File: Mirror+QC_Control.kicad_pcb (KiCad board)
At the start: 2 copper layers, 48.5 x 84 mm, 29 parts, among them J1 3220-10-0300-00, J2 Screw_Terminal_01x04, J3 Screw_Terminal_01x06, U1 LT1012, U10 LT1012, U11 LT1012, U2 LM4040DBZ-2.0, U3 LT1012, U4 LM4040DBZ-2.0, U5 LT1012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

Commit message: changes after DR1
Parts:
- added C10: 0.1muF, Capacitor_SMD:C_0805_2012Metric, F.Cu at (118.4, 38.3)
- added C11: 0.1muF, Capacitor_SMD:C_0805_2012Metric, F.Cu at (103.5, 88.4)
- added C12: 0.1muF, Capacitor_SMD:C_0805_2012Metric, F.Cu at (94.0, 100.5)
- added C13: 0.1muF, Capacitor_SMD:C_0805_2012Metric, F.Cu at (119.2, 98.4)
- added C14: 0.1muF, Capacitor_SMD:C_0805_2012Metric, F.Cu at (74.4, 113.8)
- added C15: 0.1muF, Capacitor_SMD:C_0805_2012Metric, F.Cu at (104.6, 115.5)
- added C16: C, Capacitor_SMD:C_0805_2012Metric, F.Cu at (115.4, 59.3)
- added C17: C, Capacitor_SMD:C_0805_2012Metric, F.Cu at (115.4, 91.4)
- added C18: C, Capacitor_SMD:C_0805_2012Metric, F.Cu at (117.3, 115.9)
- added C4: 0.1muF, Capacitor_SMD:C_0805_2012Metric, F.Cu at (93.1, 35.0)
- added C5: 0.1muF, Capacitor_SMD:C_0805_2012Metric, F.Cu at (74.2, 56.2)
- added C6: 0.1muF, Capacitor_SMD:C_0805_2012Metric, F.Cu at (105.5, 56.0)
- added C7: 0.1muF, Capacitor_SMD:C_0805_2012Metric, F.Cu at (96.5, 72.5)
- added C8: 0.1muF, Capacitor_SMD:C_0805_2012Metric, F.Cu at (119.5, 69.9)
- added C9: 0.1muF, Capacitor_SMD:C_0805_2012Metric, F.Cu at (76.5, 88.9)
- added D1: 5962-XL-2012UGCTR-ND, LED_SMD:LED_0805_2012Metric, F.Cu at (38.0, 117.0)
- added D2: 5962-XL-2012UGCTR-ND, LED_SMD:LED_0805_2012Metric, F.Cu at (38.0, 112.5)
- added D3: 5962-XL-2012UGCTR-ND, LED_SMD:LED_0805_2012Metric, F.Cu at (37.9, 107.5)
- added GND: TestPoint, TestPoint:TestPoint_Pad_2.0x2.0mm, F.Cu at (111.0, 117.0)
- added GND: TestPoint, TestPoint:TestPoint_Pad_2.0x2.0mm, F.Cu at (107.5, 62.5)
- added GND: TestPoint, TestPoint:TestPoint_Pad_2.0x2.0mm, F.Cu at (110.5, 91.5)
- added H1: MountingHole_Pad_MP, MountingHole:MountingHole_3.2mm_M3_DIN965_Pad_TopBottom, F.Cu at (26.0, 33.0)
- added H2: MountingHole_Pad_MP, MountingHole:MountingHole_3.2mm_M3_DIN965_Pad_TopBottom, F.Cu at (25.5, 114.0)
- added H3: MountingHole_Pad_MP, MountingHole:MountingHole_3.2mm_M3_DIN965_Pad_TopBottom, F.Cu at (167.5, 30.5)
- added H4: MountingHole_Pad_MP, MountingHole:MountingHole_3.2mm_M3_DIN965_Pad_TopBottom, F.Cu at (166.0, 113.5)
- added R13: 1300, Resistor_SMD:R_0805_2012Metric, F.Cu at (43.2, 117.0)
- added R14: 1300, Resistor_SMD:R_0805_2012Metric, F.Cu at (43.0, 112.5)
- added R17: 300, Resistor_SMD:R_0805_2012Metric, F.Cu at (43.0, 107.5)
- added SUM: 0-(-3.3V): TestPoint, TestPoint:TestPoint_Pad_2.0x2.0mm, F.Cu at (95.0, 112.0)
- added SUM: 0-3.3V: TestPoint, TestPoint:TestPoint_Pad_2.0x2.0mm, F.Cu at (126.7, 116.4)
- added X: 0-(-3.3V): TestPoint, TestPoint:TestPoint_Pad_2.0x2.0mm, F.Cu at (95.5, 56.5)
- added X: 0-3.3V: TestPoint, TestPoint:TestPoint_Pad_2.0x2.0mm, F.Cu at (127.1, 56.5)
- added Y: 0-(-3.3V): TestPoint, TestPoint:TestPoint_Pad_2.0x2.0mm, F.Cu at (96.5, 82.5)
- added Y: 0-3.3V: TestPoint, TestPoint:TestPoint_Pad_2.0x2.0mm, F.Cu at (127.5, 87.4)
- J1: value 3220-10-0300-00 -> FSM
- moved U11 119.2 mm to (115.5, 44.4), turned to 0 degrees
- moved U2 115.5 mm to (62.1, 44.6)
- moved R3 112.8 mm to (71.2, 43.6), turned to 0 degrees
- moved R5 103.9 mm to (105.1, 43.5), turned to 0 degrees
- moved R6 103.2 mm to (115.5, 55.5), turned to 0 degrees
- moved U10 102.3 mm to (88.2, 44.1), turned to 0 degrees
- moved J1 101.3 mm to (156.5, 85.0), turned to -90 degrees
- moved U7 98.7 mm to (156.0, 52.1), turned to -90 degrees
- moved C1 96.4 mm to (88.2, 59.5), turned to 0 degrees
- moved R2 96.2 mm to (88.2, 55.2), turned to 0 degrees
- moved R1 92.0 mm to (71.2, 51.6), turned to 0 degrees
- moved J2 88.8 mm to (40.0, 81.0), turned to -90 degrees
- moved J3 68.5 mm to (40.0, 46.2), turned to -90 degrees
- moved U3 68.4 mm to (115.5, 76.4), turned to 0 degrees
- moved R10 63.9 mm to (103.6, 76.0), turned to 0 degrees
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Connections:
- net Net-(C1-Pad2) renamed /x_stage1
- net Net-(C2-Pad2) renamed /y_stage1
- net Net-(C3-Pad2) renamed /sum_stage1
- net Net-(U7-14_A0_TX3_SPDIF_OUT) renamed /x_stage2
- net Net-(U7-15_A1_RX3_SPDIF_IN) renamed /y_stage2
- net Net-(U7-16_A2_RX4_SCL1) renamed /sum_stage2
- U7 pad 1: unconnected-(U7-GND-Pad1) -> GND
- U7 pad 17: unconnected-(U7-GND-Pad17) -> GND
- U7 pad 33: +5V -> unconnected-(U7-VIN-Pad33)
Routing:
- net GND: track 91.7 -> 557.3 mm, vias 7 -> 24
- net +15V: track 97.8 -> 333.9 mm, vias 6 -> 12
- net -15V: track 132.8 -> 326.6 mm, vias 6 -> 11
- net +5V: track 68.7 -> 189.0 mm
- net /sum_stage2: track 24.6 -> 108.7 mm
- net /y_stage2: track 29.7 -> 97.7 mm
- net /x+: track 75.9 -> 32.5 mm, vias 0 -> 2
- net /sum: track 19.4 -> 59.5 mm, vias 0 -> 2
- net /SCLK: track 60.3 -> 22.1 mm
- net /x_stage2: track 55.3 -> 89.8 mm, vias 0 -> 2
- net Net-(U1--): track 28.4 -> 49.9 mm, vias 0 -> 2
- net /DIN: track 61.6 -> 41.7 mm
- net Net-(U5--): track 19.3 -> 38.1 mm, vias 0 -> 2
- net Net-(U10--): track 22.6 -> 40.9 mm, vias 0 -> 2
- net /y_stage1: track 22.6 -> 32.3 mm
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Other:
- board size 48.5 x 84 mm -> 152.5 x 96.5 mm
- board text added: "+-10V to 0-(-3.3V)"
- board text added: "+15V"
- board text added: "+5V"
- board text added: "-15V"
- board text added: "0-(-3.3V) to 0-3.3V"
- board text added: "FSM PINS: 1: N/C 2: N/C 3: +5V 4: GND 5: EN 6: DIN 7: CS 8: CLK 9: FCLKX 10: FCLKY"
- board text added: "GND"
- board text added: "POWER"
- board text added: "QUADCELL"
- board text added: "SUM"
- board text added: "SUM 2-Stage Conversion 0-10V to 0-3.3V"
- board text added: "TEENSY PINS a0: x+ a1: y+ a2: sum 5: EN 7: SPI SYNC 9: FCLK_X 10: FCLK_Y 11: SPI DATA 13: SPI CLOCK"
- board text added: "X+"
- board text added: "X+ 2-Stage Conversion +-10V to 0-3.3V"
- board text added: "Y+"
- board text added: "Y+ 2-Stage Conversion +-10V to 0-3.3V"
- board text added: "paigefor@mit.edu"

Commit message: changes since DR2
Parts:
- removed U4: LM4040DBZ-2.0, Package_TO_SOT_SMD:SOT-23
- added GND4: TP_GND4, TestPoint:TestPoint_Loop_D3.50mm_Drill1.4mm_Beaded, F.Cu at (138.5, 91.5)
- added R18: 750, Capacitor_SMD:C_0805_2012Metric, F.Cu at (70.0, 44.0)
- added R19: 10k, Capacitor_SMD:C_0805_2012Metric, F.Cu at (73.0, 44.0)
- added R20: 750, Capacitor_SMD:C_0805_2012Metric, F.Cu at (70.5, 71.5)
- added R21: 10k, Capacitor_SMD:C_0805_2012Metric, F.Cu at (77.0, 71.5)
- added TP_DIN1: TP_DIN, TestPoint:TestPoint_Loop_D3.50mm_Drill1.4mm_Beaded, F.Cu at (138.5, 86.0)
- added TP_EN1: TP_EN, TestPoint:TestPoint_Loop_D3.50mm_Drill1.4mm_Beaded, F.Cu at (138.0, 79.0)
- added TP_SYNC1: TP_SYNC, TestPoint:TestPoint_Loop_D3.50mm_Drill1.4mm_Beaded, F.Cu at (138.0, 72.5)
- added U8: LM4040DBZ-2.0, Package_TO_SOT_SMD:SOT-23, F.Cu at (74.0, 71.5)
- C10, C11, C12, C13, C14, C15, C4, C5, C6, C7, C8, C9: value 0.1muF -> 0.1uF
- GND1: renamed from GND; value TestPoint -> TP_GND1; footprint TestPoint:TestPoint_Pad_2.0x2.0mm -> TestPoint:TestPoint_Loop_D3.50mm_Drill1.4mm_Beaded
- GND2: renamed from GND; value TestPoint -> TP_GND2; footprint TestPoint:TestPoint_Pad_2.0x2.0mm -> TestPoint:TestPoint_Loop_D3.50mm_Drill1.4mm_Beaded
- GND3: renamed from GND; value TestPoint -> TP_GND3; footprint TestPoint:TestPoint_Pad_2.0x2.0mm -> TestPoint:TestPoint_Loop_D3.50mm_Drill1.4mm_Beaded
- J1: value FSM -> FSM Driver
- SumStage1: renamed from SUM: 0-(-3.3V); value TestPoint -> TP_sumstage1; footprint TestPoint:TestPoint_Pad_2.0x2.0mm -> TestPoint:TestPoint_Loop_D3.50mm_Drill1.4mm_Beaded
- SumStage2: renamed from SUM: 0-3.3V; value TestPoint -> TP_sumstage2; footprint TestPoint:TestPoint_Pad_2.0x2.0mm -> TestPoint:TestPoint_Loop_D3.50mm_Drill1.4mm_Beaded
- XStage1: renamed from X: 0-(-3.3V); value TestPoint -> TP_xstage1; footprint TestPoint:TestPoint_Pad_2.0x2.0mm -> TestPoint:TestPoint_Loop_D3.50mm_Drill1.4mm_Beaded
- XStage2: renamed from X: 0-3.3V; value TestPoint -> TP_xstage2; footprint TestPoint:TestPoint_Pad_2.0x2.0mm -> TestPoint:TestPoint_Loop_D3.50mm_Drill1.4mm_Beaded
- YStage1: renamed from Y: 0-(-3.3V); value TestPoint -> TP_ystage1; footprint TestPoint:TestPoint_Pad_2.0x2.0mm -> TestPoint:TestPoint_Loop_D3.50mm_Drill1.4mm_Beaded
- YStage2: renamed from Y: 0-3.3V; value TestPoint -> TP_ystage2; footprint TestPoint:TestPoint_Pad_2.0x2.0mm -> TestPoint:TestPoint_Loop_D3.50mm_Drill1.4mm_Beaded
- moved J1 31.7 mm to (126.0, 76.5)
- moved GND3 29.7 mm to (98.0, 90.3)
- moved GND2 28.4 mm to (97.0, 66.5)
- moved GND1 26.1 mm to (98.5, 38.0)
- moved U7 25.8 mm to (130.4, 49.5)
- moved D1 24.4 mm to (55.6, 100.0)
- moved R13 23.7 mm to (59.8, 100.0)
- moved D2 23.7 mm to (55.5, 96.5), turned to 0 degrees
- moved H4 23.3 mm to (146.0, 101.5)
- moved R14 23.1 mm to (59.6, 96.5)
- moved D3 22.7 mm to (55.4, 93.0)
- moved SumStage2 22.1 mm to (111.0, 100.8)
- moved R17 22.0 mm to (59.6, 93.0)
- moved H2 21.6 mm to (43.5, 102.0)
- moved H3 21.6 mm to (146.0, 28.5)
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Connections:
- D2 pad 1: Net-(D2-K) -> -15V
- D2 pad 2: -15V -> Net-(D2-A)
- R14 pad 1: Net-(D2-K) -> Net-(D2-A)
- U2 pad 2: +5V -> GND
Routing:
- net GND: track 557.3 -> 409.8 mm, vias 24 -> 19
- net -15V: track 326.6 -> 216.7 mm, vias 11 -> 10
- net +15V: track 333.9 -> 238.7 mm, vias 12 -> 9
- net +5V: track 189.0 -> 131.0 mm, vias 3 -> 6
- net Net-(U1--): track 49.9 -> 13.6 mm
- net /y_stage2: track 97.7 -> 69.9 mm, vias 0 -> 2
- net Net-(U10--): track 40.9 -> 14.1 mm
- net /FCLK_Y: track 58.4 -> 34.0 mm
- net /sum_stage2: track 108.7 -> 88.3 mm, vias 0 -> 2
- net Net-(U5--): track 38.1 -> 17.9 mm
- net /FCLK_X: track 48.3 -> 30.5 mm
- net /x_stage1: track 36.0 -> 18.8 mm, vias 0 -> 2
- net Net-(U3--): track 27.1 -> 11.7 mm
- net /y_stage1: track 32.3 -> 19.4 mm
- net Net-(U11--): track 25.9 -> 14.5 mm
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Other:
- board size 152.5 x 96.5 mm -> 112.5 x 82 mm
- board text added: "DIN"
- board text added: "EN"
- board text added: "FCLK_X"
- board text added: "FCLK_Y"
- board text added: "N/C"
- board text added: "Paige Forester paigefor@mit.edu"
- board text added: "QC INPUT"
- board text added: "QC OUTPUT"
- board text added: "Quadcell Feedback and FSM Control with Teensy 4.0"
- board text added: "SCLK"
- board text added: "SUM Dual Stage Conversion of 0-10V to 0-3.3V"
- board text added: "SYNC"
- board text added: "Teensy 4.0"
- board text added: "X+ Dual Stage Conversion of +-10V to 0-3.3V"
- board text added: "Y+ Dual Stage Conversion of +-10V to 0-3.3V"
- board text removed: "FSM PINS: 1: N/C 2: N/C 3: +5V 4: GND 5: EN 6: DIN 7: CS 8: CLK 9: FCLKX 10: FCLKY"
- board text removed: "SUM 2-Stage Conversion 0-10V to 0-3.3V"
- board text removed: "X+ 2-Stage Conversion +-10V to 0-3.3V"
- board text removed: "Y+ 2-Stage Conversion +-10V to 0-3.3V"
- board text removed: "paigefor@mit.edu"

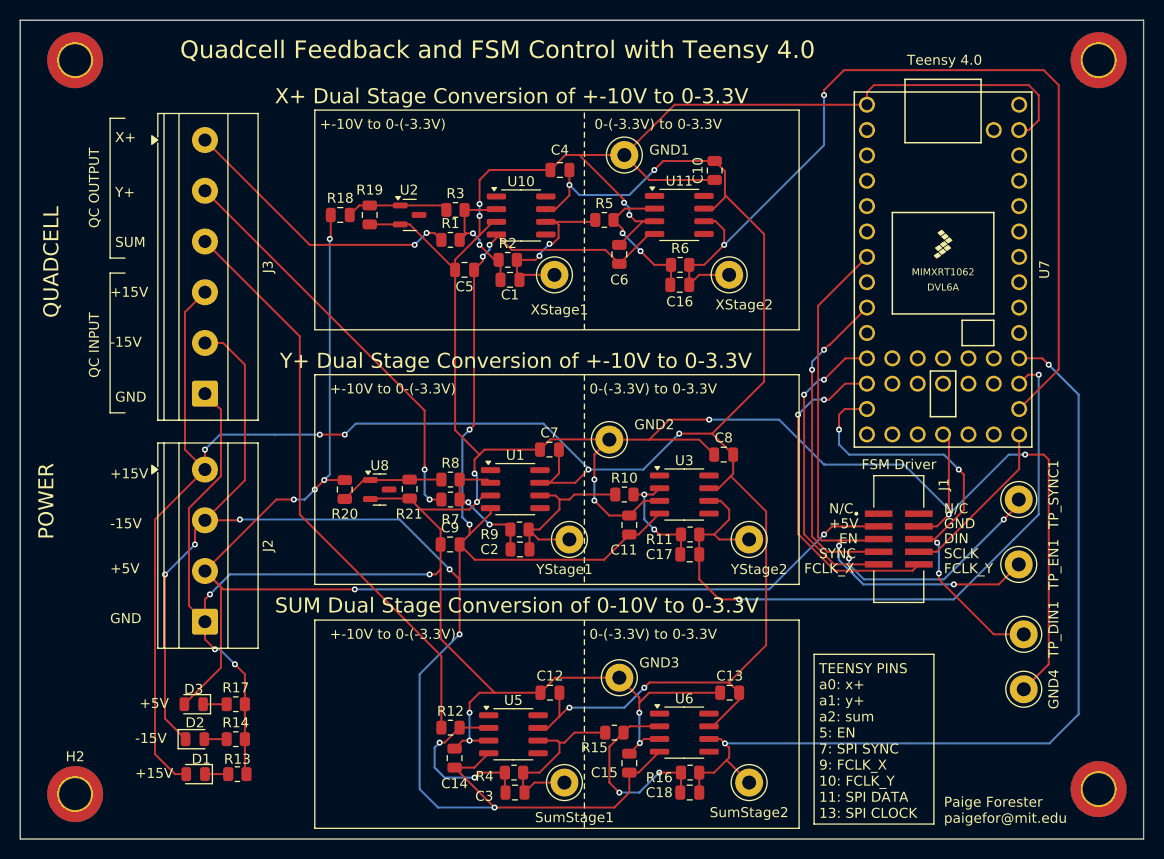
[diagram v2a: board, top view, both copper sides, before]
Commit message: added LCSC values and refined silkscreen. still missing capacitor values for LPFs
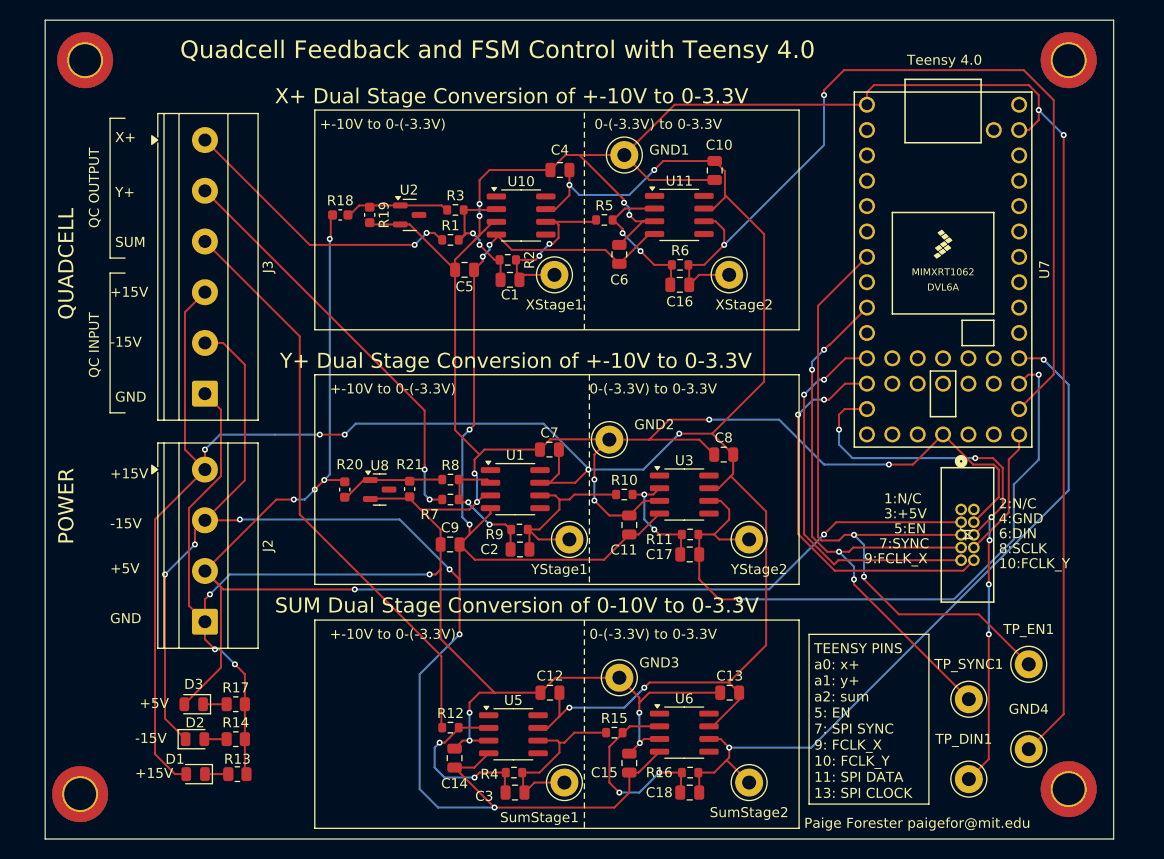
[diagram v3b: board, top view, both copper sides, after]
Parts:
- removed J1: FSM Driver, 3220-10-0300-00:CNC_3220-10-0300-00
- added J4: FSM DRIVER, FSM:CONN_3220-10-0100-00_CNC, F.Cu at (132.2, 73.5)
- R1, R10, R11, R12, R15, R16, R2, R3, R4, R5, R6, R7, R8, R9: footprint Resistor_SMD:R_0805_2012Metric -> Resistor_SMD:R_0603_1608Metric
- R18, R19, R20, R21: footprint Capacitor_SMD:C_0805_2012Metric -> Capacitor_SMD:C_0603_1608Metric
- moved TP_SYNC1 20.6 mm to (133.0, 92.5), turned to 180 degrees
- moved TP_DIN1 15.5 mm to (133.0, 100.5), turned to 180 degrees
- moved TP_EN1 10.0 mm to (139.0, 89.0), turned to 180 degrees
- moved GND4 6.02 mm to (139.0, 97.5), turned to 180 degrees
- moved H3 3.00 mm to (143.0, 28.5)
- moved H4 3.00 mm to (143.0, 101.5)
- moved H1 1.00 mm to (44.5, 28.5)
- moved H2 0.50 mm to (44.0, 102.0)
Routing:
- net GND: track 409.8 -> 439.5 mm, vias 19 -> 20
- net /sum_stage2: track 88.3 -> 73.5 mm
- net /DIN: track 45.5 -> 58.5 mm, vias 4 -> 6
- net /EN: track 58.6 -> 69.7 mm
- net +5V: track 131.0 -> 139.4 mm
- net /FCLK_X: track 30.5 -> 38.9 mm
- net /SYNC: track 55.1 -> 61.1 mm
- net /FCLK_Y: track 34.0 -> 39.7 mm
- net /SCLK: track 16.9 -> 13.2 mm
- net /x_stage2: track 93.3 -> 91.7 mm
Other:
- board size 112.5 x 82 mm -> 107 x 82 mm
- board text added: "10:FCLK_Y"
- board text added: "1:N/C"
- board text added: "2:N/C"
- board text added: "3:+5V"
- board text added: "4:GND"
- board text added: "5:EN"
- board text added: "6:DIN"
- board text added: "7:SYNC"
- board text added: "8:SCLK"
- board text added: "9:FCLK_X"
- board text removed: "DIN"
- board text removed: "EN"
- board text removed: "FCLK_X"
- board text removed: "FCLK_Y"
- board text removed: "N/C"
- board text removed: "SCLK"
- board text removed: "SYNC"

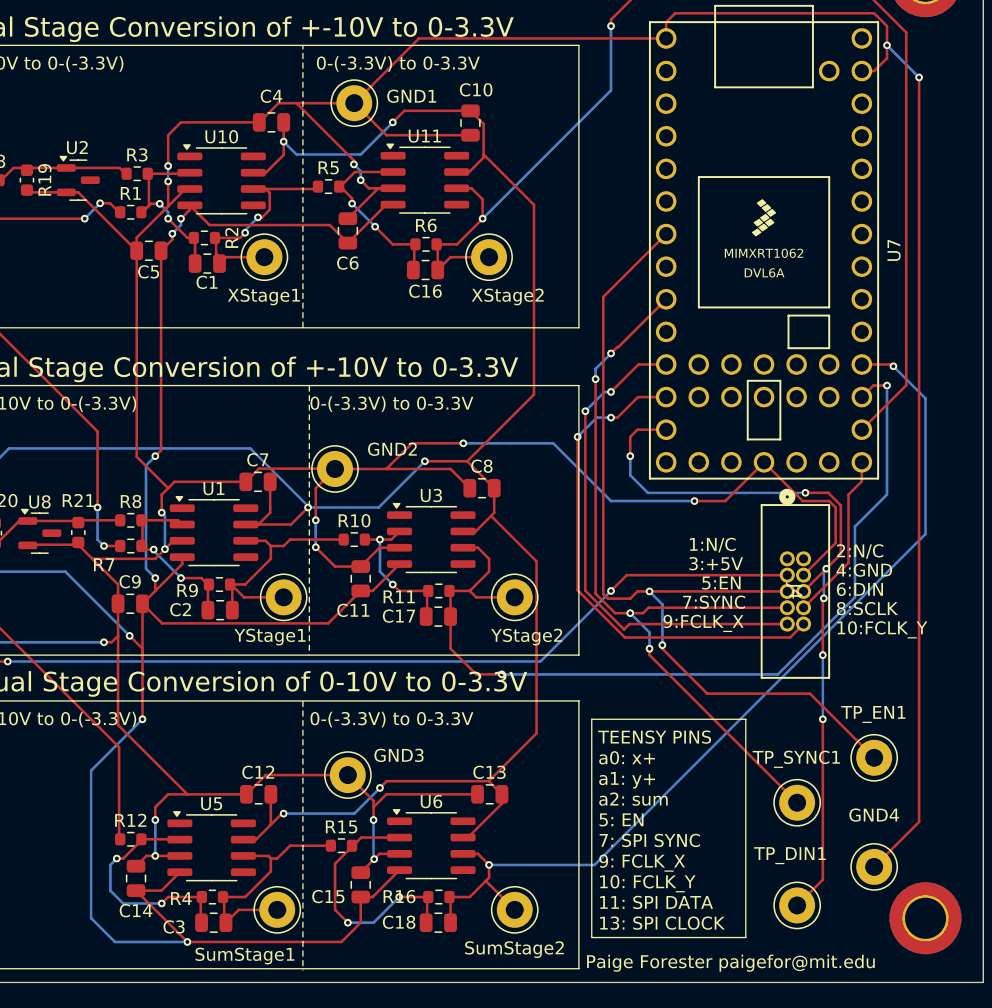
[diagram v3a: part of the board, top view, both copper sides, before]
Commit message: changes include capacitance values for LPFs
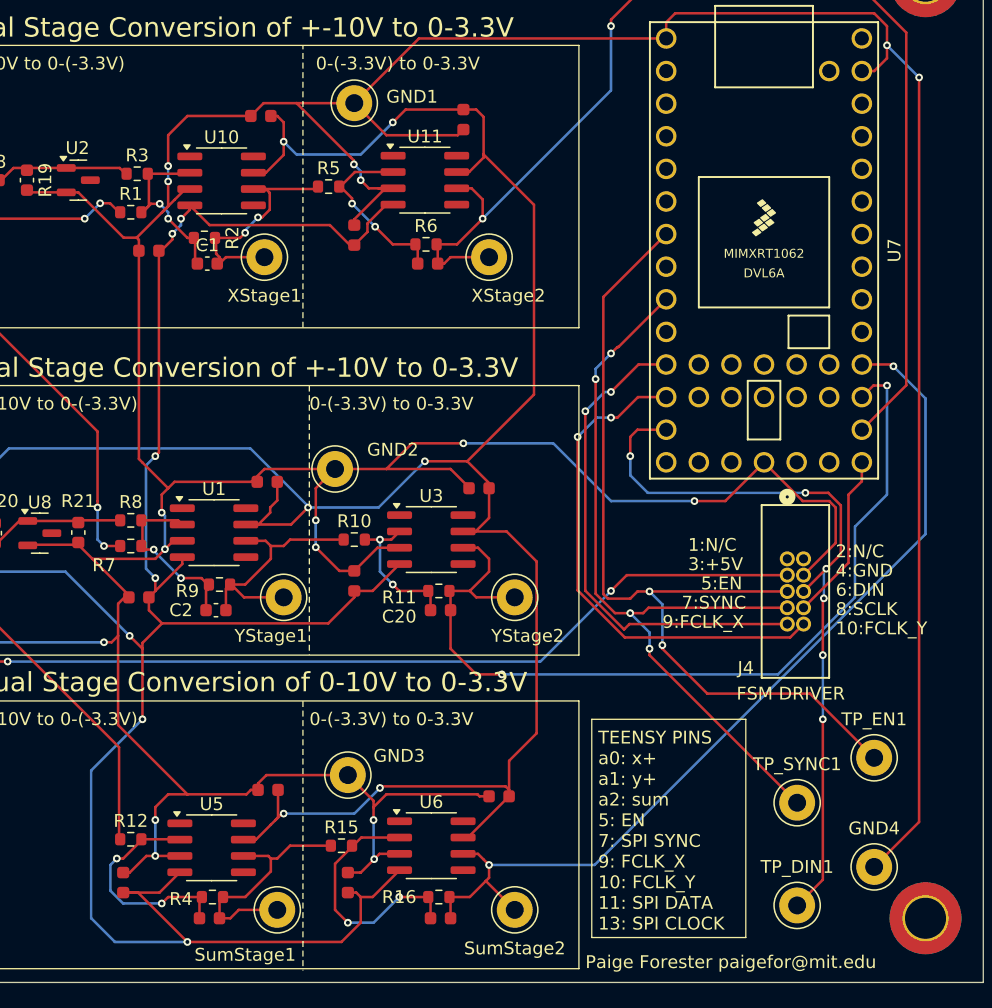
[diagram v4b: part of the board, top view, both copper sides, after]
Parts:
- removed C17, C18, C3: C, Capacitor_SMD:C_0805_2012Metric
- added C19: 100nF, PCM_JLCPCB:C_0603, F.Cu at (109.8, 92.0)
- added C20: 2.2nF, PCM_JLCPCB:C_0603, F.Cu at (105.2, 77.5)
- added C21: 2.2nF, PCM_JLCPCB:C_0603, F.Cu at (105.2, 101.5)
- C1, C2: value C -> 12nF; footprint Capacitor_SMD:C_0805_2012Metric -> Capacitor_SMD:C_0603_1608Metric
- C10, C11, C12, C13, C14, C4, C5, C6, C7, C8, C9: value 0.1uF -> 100nF; footprint Capacitor_SMD:C_0805_2012Metric -> PCM_JLCPCB:C_0603
- C15: value 0.1uF -> 2.2nF; footprint Capacitor_SMD:C_0805_2012Metric -> PCM_JLCPCB:C_0603
- C16: value C -> 6.8nF; footprint Capacitor_SMD:C_0805_2012Metric -> PCM_JLCPCB:C_0603
- moved C16 53.2 mm to (87.2, 101.5)
- moved C15 48.7 mm to (104.2, 50.5), turned to 0 degrees
- moved C13 13.0 mm to (98.0, 98.7), turned to 90 degrees
- moved C14 1.05 mm to (80.5, 98.7), turned to 90 degrees
- moved C4 0.97 mm to (91.2, 39.0)
- moved C9 0.84 mm to (81.7, 76.5), turned to 180 degrees
- moved C12 0.81 mm to (91.8, 91.5)
- moved C7 0.72 mm to (91.7, 67.5)
- moved C10 0.61 mm to (107.0, 39.3), turned to -90 degrees
- moved C6 0.60 mm to (98.5, 48.3), turned to 90 degrees
- moved C11 0.53 mm to (98.5, 75.2), turned to 90 degrees
- moved C2 0.33 mm to (87.7, 77.5), turned to 180 degrees
- moved C8 0.23 mm to (108.2, 68.0), turned to 180 degrees
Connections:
- C10 pad 1: GND -> +15V
- C10 pad 2: +15V -> GND
- C11 pad 1: GND -> -15V
- C11 pad 2: -15V -> GND
- C13 pad 1: GND -> -15V
- C13 pad 2: +15V -> GND
- C14 pad 1: GND -> -15V
- C14 pad 2: -15V -> GND
- C15 pad 1: GND -> Net-(U11--)
- C15 pad 2: -15V -> /x_stage2
- C16 pad 1: Net-(U11--) -> Net-(U5--)
- C16 pad 2: /x_stage2 -> /sum_stage1
- C2 pad 1: Net-(U1--) -> /y_stage1
- C2 pad 2: /y_stage1 -> Net-(U1--)
- C6 pad 1: GND -> -15V
- C6 pad 2: -15V -> GND
- C8 pad 1: GND -> +15V
- C8 pad 2: +15V -> GND
- C9 pad 1: GND -> -15V
- C9 pad 2: -15V -> GND
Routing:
- net GND: track 439.5 -> 444.9 mm
- net +15V: track 238.7 -> 243.0 mm
- net -15V: track 216.7 -> 219.0 mm
- net /x_stage2: track 91.7 -> 91.0 mm
- net Net-(U1--): track 13.6 -> 14.1 mm
